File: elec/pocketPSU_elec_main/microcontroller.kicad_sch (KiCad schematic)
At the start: 16 parts, among them J1 Header-Male-2.54_1x20, SW3 TS-1187A-B-A-B, SW6 TS-1187A-B-A-B, U2 ESP32-S3-WROOM-1(N16R2), U3 AMS1117-3.3, U5 F.0603.00026/P2-0603B1TS2-06T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

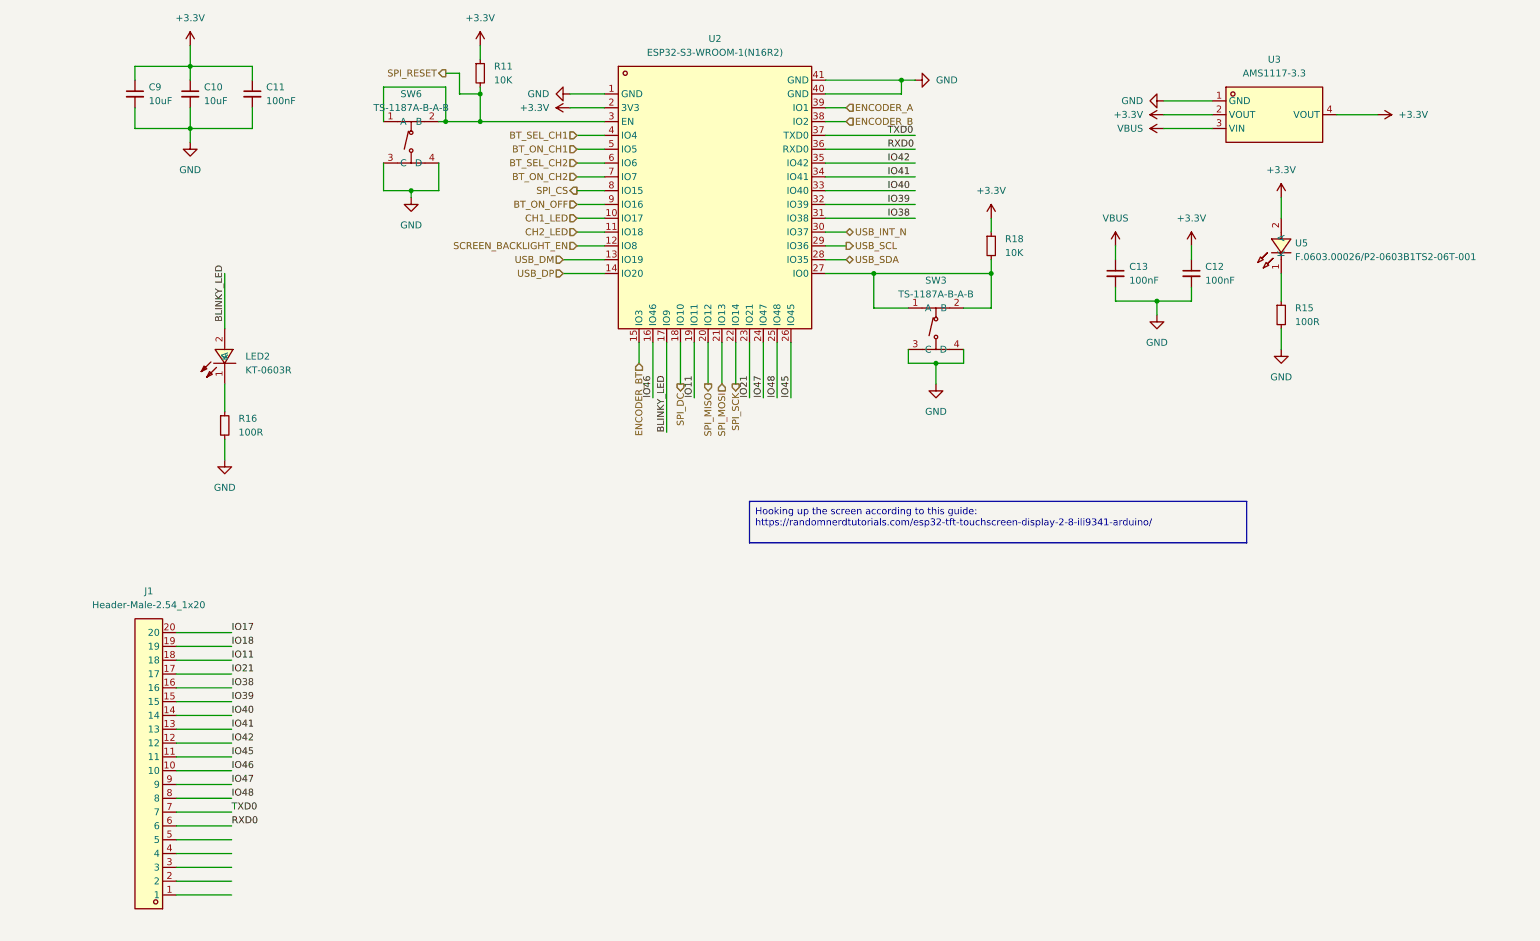
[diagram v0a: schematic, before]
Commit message: Cleanup, Buck, CAN (#6)
* mid-layout

* finished routing

* Kibot (#7)

Add kibot with JLC output generation

* fix 3d, add drc

* fix erc

* fix pcb drc

* drc ignore_unconnected

* attempt to add githash and tag

* add silk githash string

* add silk tag string

* change outputs

---------

Co-authored-by: Jarrod Tuma <jtuma@Jarrods-Laptop.local>
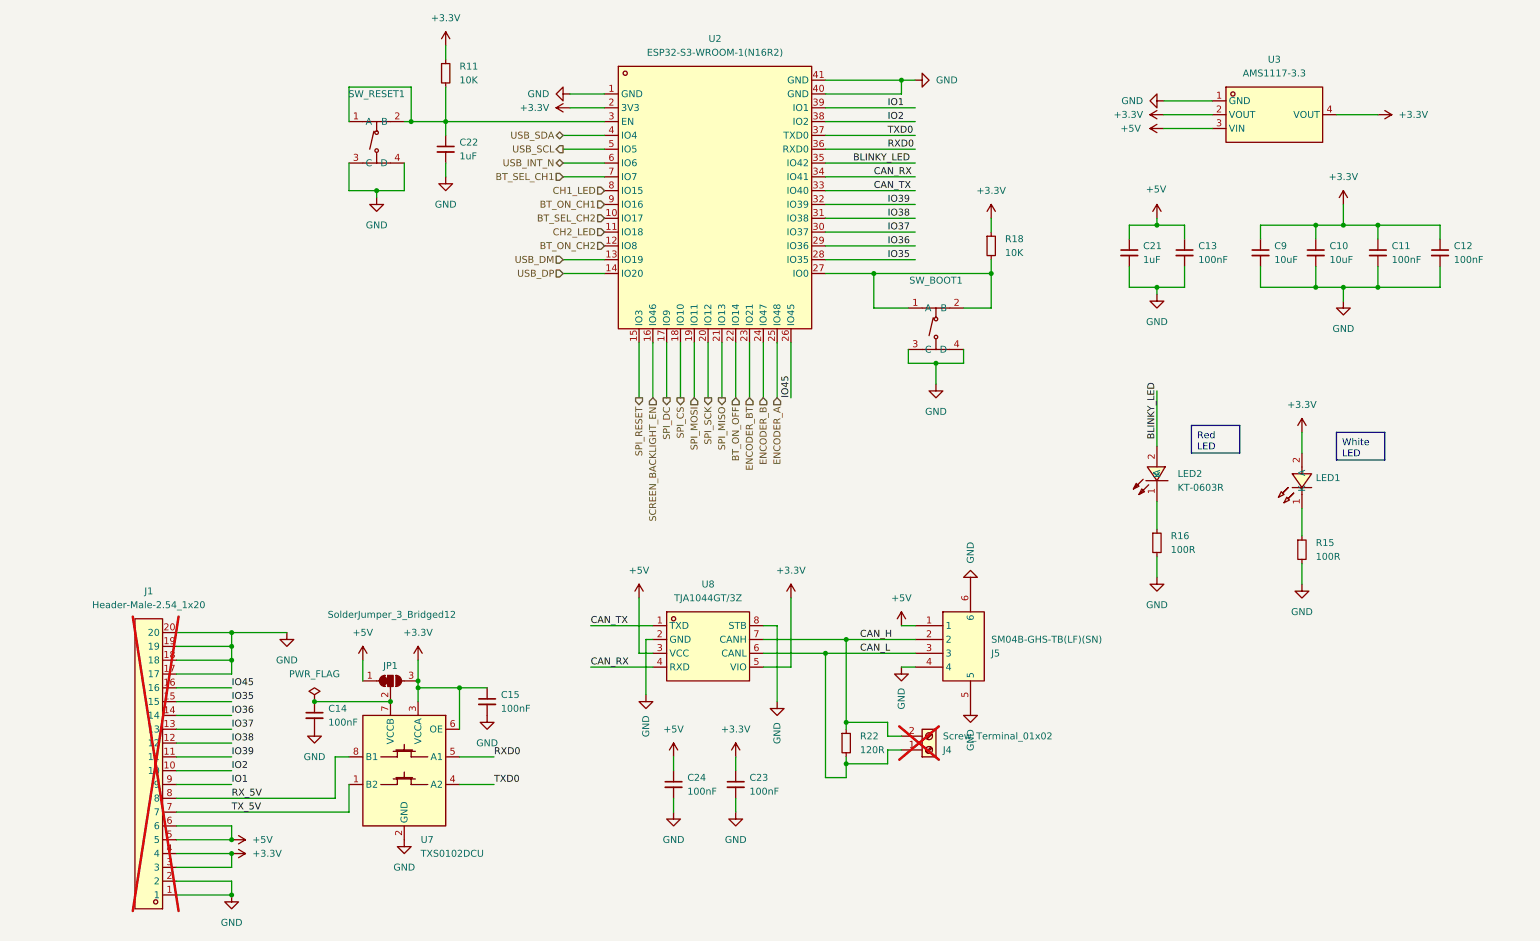
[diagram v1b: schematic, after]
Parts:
- added C14, C15, C23, C24: 100nF, Capacitor_SMD:C_0805_2012Metric, symbol Device:C_Small
- added C21, C22: 1uF, Resistor_SMD:R_0805_2012Metric, symbol Device:C_Small
- added J4: Screw_Terminal_01x02, TerminalBlock_Phoenix:TerminalBlock_Phoenix_MPT-0,5-2-2.54_1x02_P2.54mm_Horizontal, symbol Connector:Screw_Terminal_01x02
- added J5: SM04B-GHS-TB(LF)(SN), footprints:CONN-SMD_4P-P1.25_SM04B-GHS-TB-LF-SN, symbol footprints:SM04B-GHS-TB(LF)(SN)
- added JP1: SolderJumper_3_Bridged12, Jumper:SolderJumper-3_P1.3mm_Bridged12_RoundedPad1.0x1.5mm_NumberLabels, symbol Jumper:SolderJumper_3_Bridged12
- added R22: 120R, Resistor_SMD:R_0603_1608Metric, symbol Device:R_Small
- added U7: TXS0102DCU, Package_SO:VSSOP-8_2.3x2mm_P0.5mm, symbol Logic_LevelTranslator:TXS0102DCU
- added U8: TJA1044GT/3Z, footprints:SO-8_L4.9-W3.9-P1.27-LS5.9-BL, symbol footprints:TJA1044GT_3Z
- C10, C9: LCSC Part (none) -> C15850
- C11: LCSC Part (none) -> C49678
- J1: now not fitted
- LED1: renamed from U5; LCSC Part C7496819 -> C2290
- R11, R18: LCSC Part (none) -> C25744
- R15, R16: LCSC Part (none) -> C25076
- renumbered SW3 to SW_BOOT1, SW6 to SW_RESET1
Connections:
- net IO17 is gone; now on net GND: J1.20
- net IO18 is gone; now on net GND: J1.19
- net VBUS is gone; now on net +5V: C13.1, U3.3 (VIN)
- net +3.3V: now also J1.3, J1.4, C15.1, C23.1, JP1.3 (B), U7.3 (VCCA), U7.6 (OE), U8.5 (VIO)
- net BLINKY_LED: now also U2.35 (IO42); no longer U2.17 (IO9)
- net BT_ON_CH1: now also U2.9 (IO16); no longer U2.5 (IO5)
- net BT_ON_CH2: now also U2.12 (IO8); no longer U2.7 (IO7)
- net BT_ON_OFF: now also U2.22 (IO14); no longer U2.9 (IO16)
- net BT_SEL_CH1: now also U2.7 (IO7); no longer U2.4 (IO4)
- net BT_SEL_CH2: now also U2.10 (IO17); no longer U2.6 (IO6)
- net CH1_LED: now also U2.8 (IO15); no longer U2.10 (IO17)
- net ENCODER_A: now also U2.25 (IO48); no longer U2.39 (IO1)
- net ENCODER_B: now also U2.24 (IO47); no longer U2.38 (IO2)
- net ENCODER_BT: now also U2.23 (IO21); no longer U2.15 (IO3)
- net GND: now also J1.1, J1.17, J1.18, J1.2, C14.2, C15.2, C21.2, C22.2, C23.2, C24.2, J5.4, J5.5, J5.6, U7.2 (GND), U8.2 (GND), U8.8 (STB)
- net IO38: now also J1.12; no longer J1.16
- net IO39: now also J1.11; no longer J1.15
- net IO45: now also J1.16; no longer J1.11
- net RXD0: now also U7.5 (A1); no longer J1.6
- net SCREEN_BACKLIGHT_EN: now also U2.16 (IO46); no longer U2.12 (IO8)
- net SPI_CS: now also U2.18 (IO10); no longer U2.8 (IO15)
- net SPI_DC: now also U2.17 (IO9); no longer U2.18 (IO10)
- net SPI_MISO: now also U2.21 (IO13); no longer U2.20 (IO12)
- net SPI_MOSI: now also U2.19 (IO11); no longer U2.21 (IO13)
- net SPI_RESET: now also U2.15 (IO3); no longer R11.2, SW_RESET1.1 (A), SW_RESET1.2 (B), U2.3 (EN)
- net SPI_SCK: now also U2.20 (IO12); no longer U2.22 (IO14)
- net TXD0: now also U7.4 (A2); no longer J1.7
- net USB_INT_N: now also U2.6 (IO6); no longer U2.30 (IO37)
- net USB_SCL: now also U2.5 (IO5); no longer U2.29 (IO36)
- net USB_SDA: now also U2.4 (IO4); no longer U2.28 (IO35)
- net +5V: now reaches J1.5
- net +5V: now also J1.6, C21.1, C24.1, J5.1, JP1.1 (A), U8.3 (VCC)
- removed net IO11: J1.18, U2.19 (IO11)
- removed net IO21: J1.17, U2.23 (IO21)
- net IO40 renamed CAN_TX
- net CAN_TX: now also U8.1 (TXD); no longer J1.14
- net IO41 renamed CAN_RX
- net CAN_RX: now also U8.4 (RXD); no longer J1.13
- removed net IO42: J1.12, U2.35 (IO42)
- net IO46 renamed IO2
- net IO2: now also U2.38 (IO2); no longer U2.16 (IO46)
- net IO47 renamed IO1
- net IO1: now also U2.39 (IO1); no longer U2.24 (IO47)
- net IO48 renamed RX_5V
- net RX_5V: now also U7.8 (B1); no longer U2.25 (IO48)
- new net: C14.1, JP1.2 (C), U7.7 (VCCB)
- new net: C22.1, R11.2, SW_RESET1.1 (A), SW_RESET1.2 (B), U2.3 (EN)
- new net CAN_H: J4.2 (Pin_2), J5.2, R22.1, U8.7 (CANH)
- new net CAN_L: J4.1 (Pin_1), J5.3, R22.2, U8.6 (CANL)
- new net IO35: J1.15, U2.28 (IO35)
- new net IO36: J1.14, U2.29 (IO36)
- new net IO37: J1.13, U2.30 (IO37)
- new net TX_5V: J1.7, U7.1 (B2)
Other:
- moved on the sheet: C10, C11, C12, C13, C9, LED1, LED2, R11, R15, R16, SW_RESET1

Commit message: Add mini esp32 module, smd rotary encoder and leds
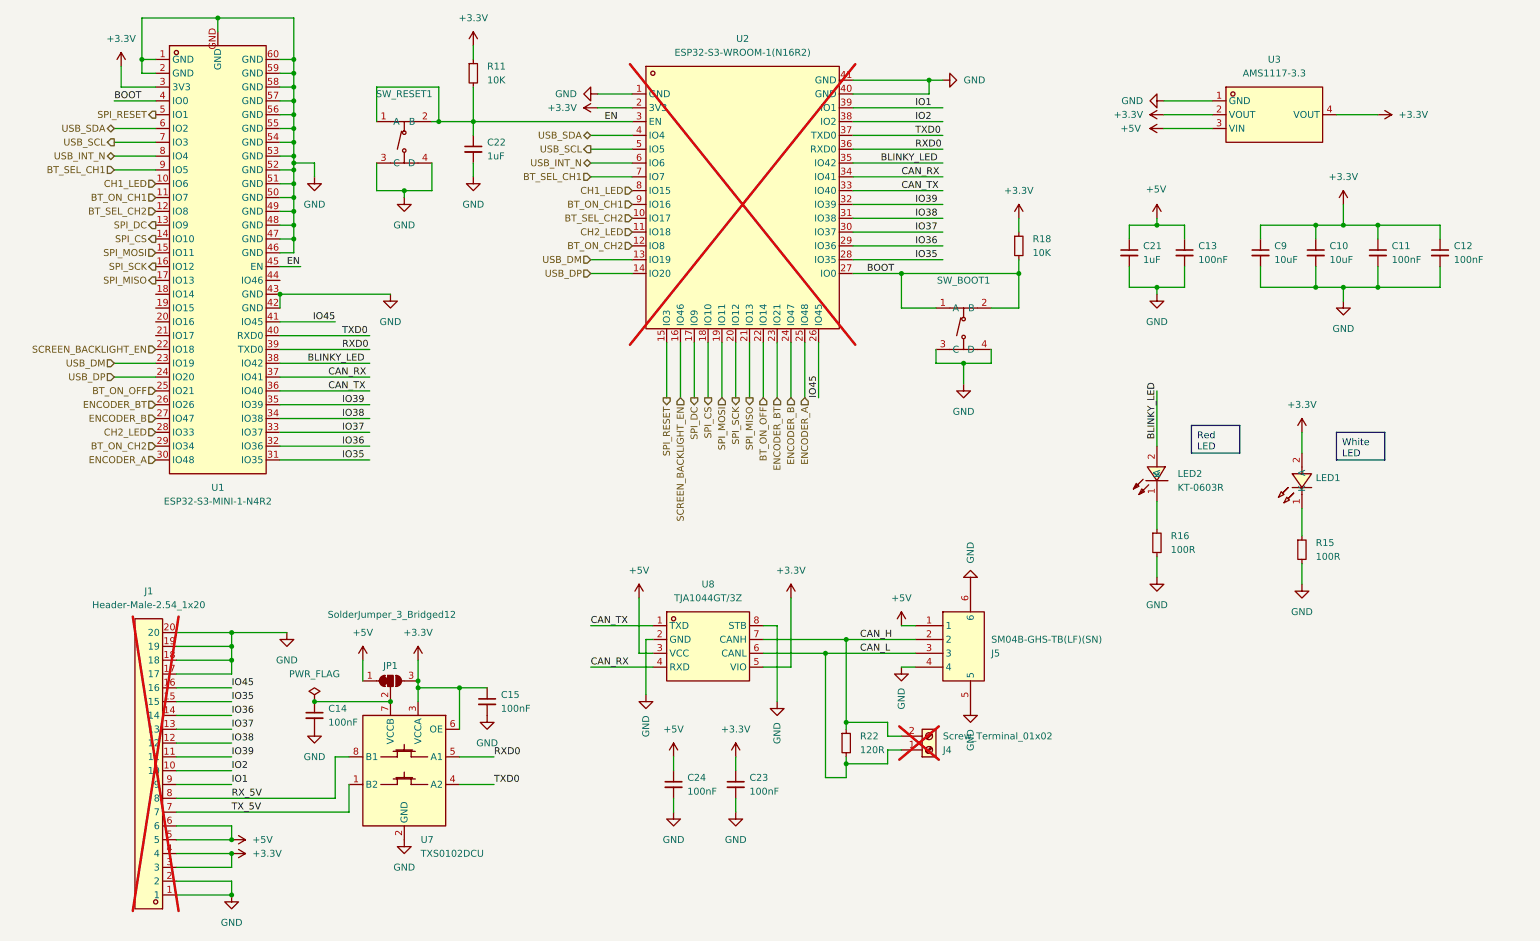
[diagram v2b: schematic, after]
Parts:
- added U1: ESP32-S3-MINI-1-N4R2, footprints:BULETM-SMD_ESP32-S3-MINI-1-N8, symbol footprints:ESP32-S3-MINI-1-N4R2
- U2: now not fitted
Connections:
- net +3.3V: now also U1.3 (3V3)
- net BLINKY_LED: now also U1.38 (IO42)
- net BT_ON_CH1: now also U1.11 (IO7)
- net BT_ON_CH2: now also U1.29 (IO34)
- net BT_ON_OFF: now also U1.25 (IO21)
- net BT_SEL_CH1: now also U1.9 (IO5)
- net BT_SEL_CH2: now also U1.12 (IO8)
- net CAN_RX: now also U1.37 (IO41)
- net CAN_TX: now also U1.36 (IO40)
- net CH1_LED: now also U1.10 (IO6)
- net CH2_LED: now also U1.28 (IO33)
- net ENCODER_A: now also U1.30 (IO48)
- net ENCODER_B: now also U1.27 (IO47)
- net ENCODER_BT: now also U1.26 (IO26)
- net GND: now also U1.1 (GND), U1.2 (GND), U1.42 (GND), U1.43 (GND), U1.46 (GND), U1.47 (GND), U1.48 (GND), U1.49 (GND), U1.50 (GND), U1.51 (GND), U1.52 (GND), U1.53 (GND), U1.54 (GND), U1.55 (GND), U1.56 (GND), U1.57 (GND), U1.58 (GND), U1.59 (GND), U1.60 (GND), U1.GND
- net IO35: now also U1.31 (IO35)
- net IO36: now also U1.32 (IO36)
- net IO37: now also U1.33 (IO37)
- net IO38: now also U1.34 (IO38)
- net IO39: now also U1.35 (IO39)
- net IO45: now also U1.41 (IO45)
- net RXD0: now also U1.39 (TXD0)
- net SCREEN_BACKLIGHT_EN: now also U1.22 (IO18)
- net SPI_CS: now also U1.14 (IO10)
- net SPI_DC: now also U1.13 (IO9)
- net SPI_MISO: now also U1.17 (IO13)
- net SPI_MOSI: now also U1.15 (IO11)
- net SPI_RESET: now also U1.5 (IO1)
- net SPI_SCK: now also U1.16 (IO12)
- net TXD0: now also U1.40 (RXD0)
- net USB_DM: now also U1.23 (IO19)
- net USB_DP: now also U1.24 (IO20)
- net USB_INT_N: now also U1.8 (IO4)
- net USB_SCL: now also U1.7 (IO3)
- net USB_SDA: now also U1.6 (IO2)
- net BOOT: now reaches R18.2, SW_BOOT1.1 (A), SW_BOOT1.2 (B), U2.27 (IO0)
- net BOOT: now also U1.4 (IO0)
- net EN: now reaches C22.1, R11.2, SW_RESET1.1 (A), SW_RESET1.2 (B), U2.3 (EN)
- net EN: now also U1.45 (EN)
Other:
- moved on the sheet: C22, R11, R18, SW_BOOT1, SW_RESET1
